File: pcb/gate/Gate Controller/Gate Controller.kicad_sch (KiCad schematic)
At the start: 0 parts

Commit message: Updated pcb
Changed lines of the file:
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@@
 	)
 	(sheet
-		(at 34.29 66.04)
+		(at 66.04 76.2)
 		(size 26.67 26.67)
 		(fields_autoplaced yes)
@@
 		)
 		(property "Sheetname" "Raspberry Box"
-			(at 34.29 65.3284 0)
+			(at 66.04 75.4884 0)
 			(effects
 				(font
@@
 		)
 		(property "Sheetfile" "RaspberryBox.kicad_sch"
-			(at 34.29 93.2946 0)
+			(at 66.04 103.4546 0)
 			(effects
 				(font

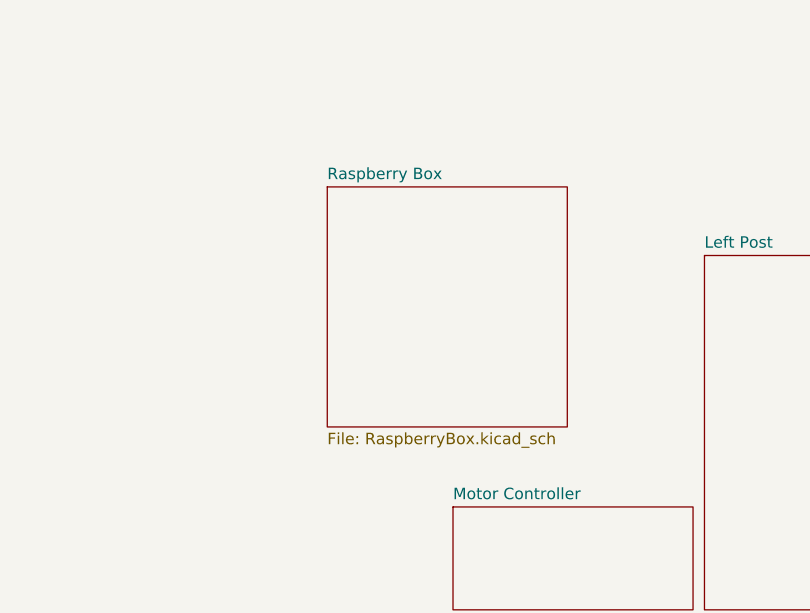
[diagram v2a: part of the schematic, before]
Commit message: reworked to add i2c pullups and reduces unusedd components
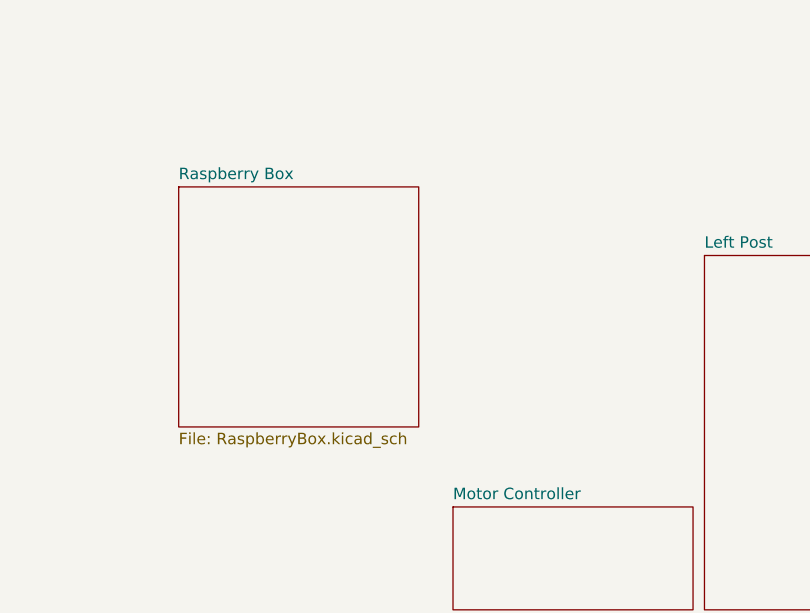
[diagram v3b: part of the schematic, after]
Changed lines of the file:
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@@
 (kicad_sch
-	(version 20231120)
+	(version 20250114)
 	(generator "eeschema")
-	(generator_version "8.0")
+	(generator_version "9.0")
 	(paper "A4")
 	(title_block
@@
 		(at 177.8 83.82)
 		(size 13.97 39.37)
+		(exclude_from_sim no)
+		(in_bom yes)
+		(on_board yes)
+		(dnp no)
 		(fields_autoplaced yes)
 		(stroke
@@
 		(at 107.95 83.82)
 		(size 13.97 39.37)
+		(exclude_from_sim no)
+		(in_bom yes)
+		(on_board yes)
+		(dnp no)
 		(fields_autoplaced yes)
 		(stroke
@@
 	)
 	(sheet
-		(at 66.04 76.2)
+		(at 49.53 76.2)
 		(size 26.67 26.67)
+		(exclude_from_sim no)
+		(in_bom yes)
+		(on_board yes)
+		(dnp no)
 		(fields_autoplaced yes)
 		(stroke
@@
 		)
 		(property "Sheetname" "Raspberry Box"
-			(at 66.04 75.4884 0)
+			(at 49.53 75.4884 0)
 			(effects
 				(font
@@
 		)
 		(property "Sheetfile" "RaspberryBox.kicad_sch"
-			(at 66.04 103.4546 0)
+			(at 49.53 103.4546 0)
 			(effects
 				(font
@@
 		(at 80.01 111.76)
 		(size 26.67 11.43)
+		(exclude_from_sim no)
+		(in_bom yes)
+		(on_board yes)
+		(dnp no)
 		(fields_autoplaced yes)
 		(stroke
@@
 		)
 	)
+	(embedded_fonts no)
 )
